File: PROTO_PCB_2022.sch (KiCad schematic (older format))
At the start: 22 parts, among them J1 HORN_EN1, J10 ECU_KILL_2, J11 ECU_KILL_3, J12 12V_EXTRA, J2 BRAKELIGHTS_EN1, J3 BRAKELIGHTS_CONN, J4 STARTER_MOTOR_EN, J5 VESC_EN_SIGNAL, J6 HORN_CONN, J7 12V_BATT1, J8 ECU_POWER_DIST, J9 ECU_KILL_1, Q1 HORN_MOSFET1, Q2 BRAKELIGHTS_MOSFET1, U1 LD1117S50TR_SOT223

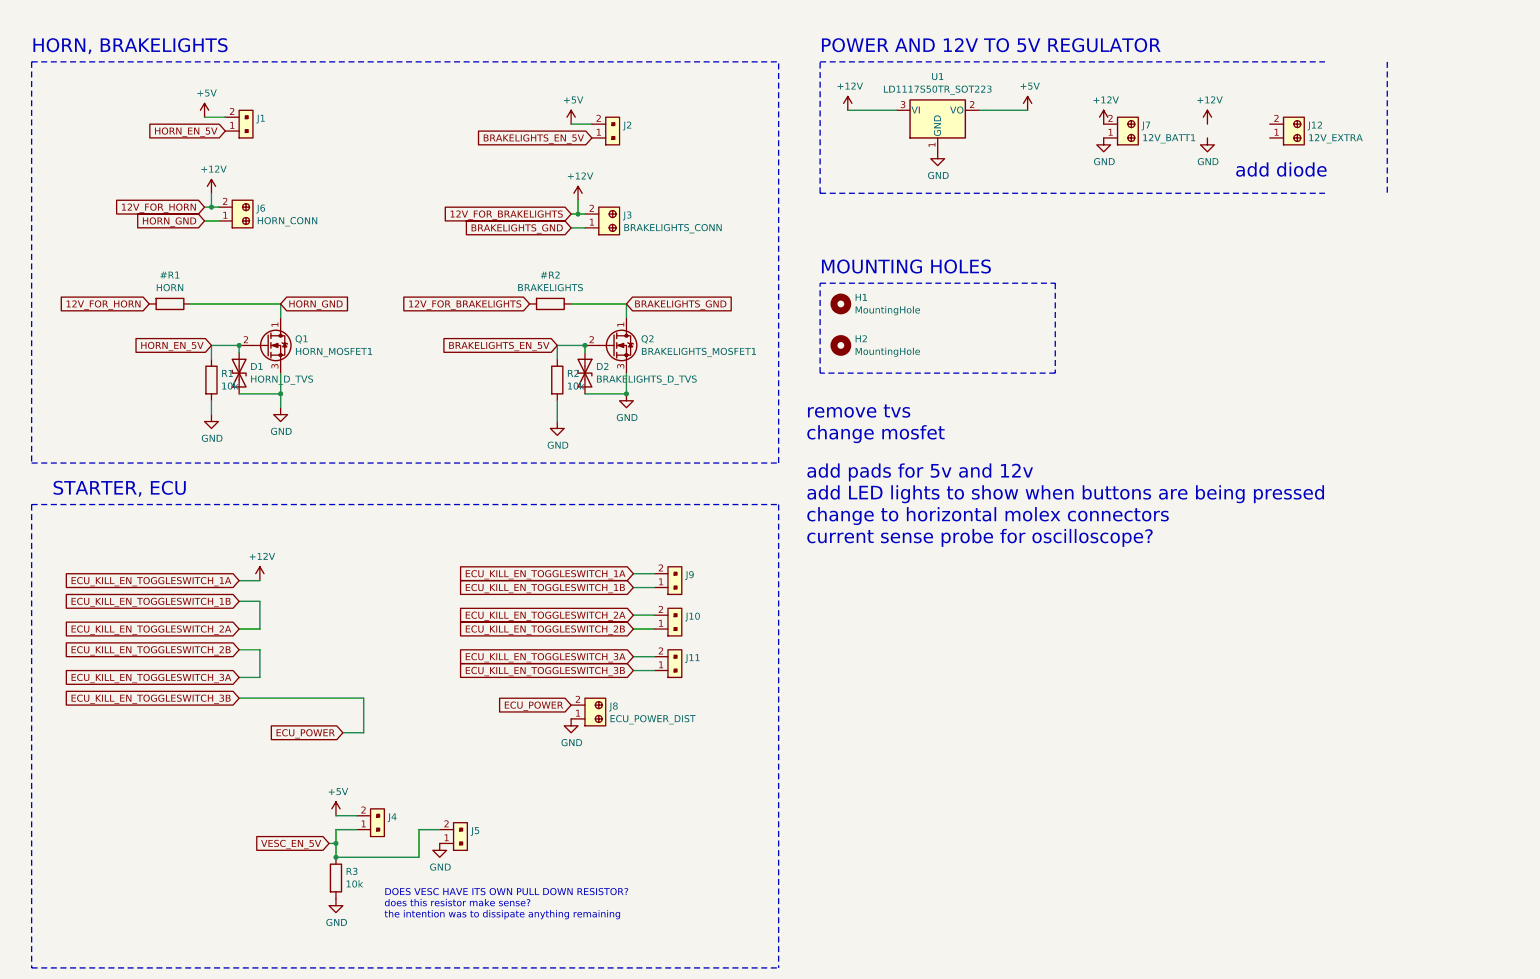
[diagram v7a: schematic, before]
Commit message: after design review edits start
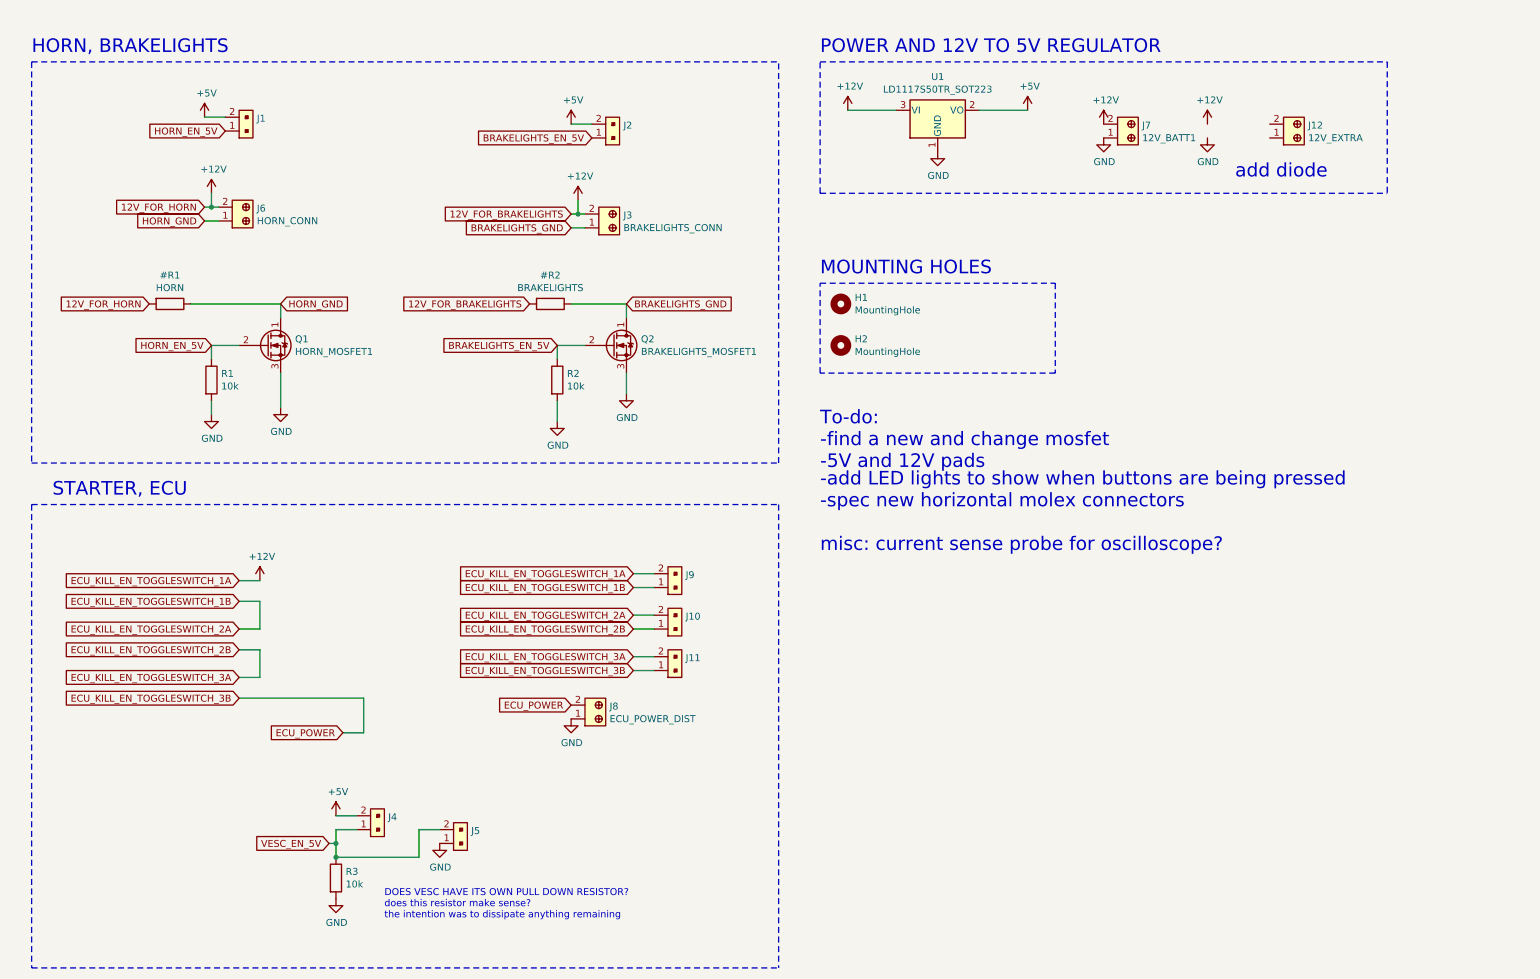
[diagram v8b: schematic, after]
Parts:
- removed D1: HORN_D_TVS, Diode_SMD:D_SMB, symbol Device:D_TVS
- removed D2: BRAKELIGHTS_D_TVS, Diode_SMD:D_SMB, symbol Device:D_TVS
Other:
- note added: "-add LED lights to show when buttons are being pressed\n-spec new horizontal molex connectors\n\nmisc: current sense probe for oscilloscope?"
- note added: "To-do:\n-find a new and change mosfet\n-5V and 12V pads\n"
- note removed: "add pads for 5v and 12v\nadd LED lights to show when buttons are being pressed\nchange to horizontal molex connectors\ncurrent sense probe for oscilloscope?"
- note removed: "remove tvs\nchange mosfet"
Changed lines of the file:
@@
 $EndComp
-$Comp
-L Device:D_TVS D2
-U 1 1 622E5E5E
-P 4800 3150
-F 0 "D2" V 4754 3230 50  0000 L CNN
-F 1 "BRAKELIGHTS_D_TVS" V 4845 3230 50  0000 L CNN
-F 2 "Diode_SMD:D_SMB" H 4800 3150 50  0001 C CNN
-F 3 "https://media.digikey.com/pdf/Data%20Sheets/AVX%20PDFs/Transient%20Suppression%20Diodes.pdf~" H 4800 3150 50  0001 C CNN
-	1    4800 3150
-	0    1    1    0
-$EndComp
-Wire Wire Line
-	4800 3000 4800 2950
-Wire Wire Line
-	4800 3300 5100 3300
-$Comp
-L Device:D_TVS D1
-U 1 1 62314A6C
-P 2300 3150
-F 0 "D1" V 2346 3070 50  0000 R CNN
-F 1 "HORN_D_TVS" V 2255 3070 50  0000 R CNN
-F 2 "Diode_SMD:D_SMB" H 2300 3150 50  0001 C CNN
-F 3 "https://media.digikey.com/pdf/Data%20Sheets/AVX%20PDFs/Transient%20Suppression%20Diodes.pdf" H 2300 3150 50  0001 C CNN
-	1    2300 3150
-	0    -1   -1   0
-$EndComp
-Wire Wire Line
-	2300 3000 2300 2950
 $Comp
 L power:GND #PWR020
@@
 Wire Wire Line
 	5100 3150 5100 3300
-Connection ~ 5100 3300
-Connection ~ 4800 2950
-$Comp
-L Device:Q_NMOS_DGS Q2
-U 1 1 618C50B5
-P 5000 2950
-F 0 "Q2" H 5205 2996 50  0000 L CNN
-F 1 "BRAKELIGHTS_MOSFET1" H 5205 2905 50  0000 L CNN
-F 2 "Package_TO_SOT_SMD:SOT-23" H 5200 3050 50  0001 C CNN
-F 3 "https://www.digikey.ca/en/products/detail/rohm-semiconductor/RK7002BMT116/4924083" H 5000 2950 50  0001 C CNN
-F 4 "RK7002BMT116" H 5000 2950 50  0001 C CNN "MPN"
-F 5 "RK7002BMT116CT-ND" H 5000 2950 50  0001 C CNN "DigiKeyPN"
-	1    5000 2950
-	1    0    0    -1
-$EndComp
 Wire Wire Line
 	5100 2650 5100 2750
@@
 Wire Notes Line
 	6500 3150 6500 2500
-Wire Notes Line
-	6500 900  10150 900
-Wire Notes Line
-	6500 1850 10150 1850
 Text GLabel 2200 1400 0    50   Input ~ 0
 HORN_EN_5V
@@
 Text GLabel 4700 5550 0    50   Input ~ 0
 ECU_POWER
-Text Notes 6400 4400 0    98   ~ 0
-add pads for 5v and 12v\nadd LED lights to show when buttons are being pressed\nchange to horizontal molex connectors\ncurrent sense probe for oscilloscope?
-Connection ~ 2300 2950
 $Comp
 L Device:Q_NMOS_DGS Q1
@@
 Text GLabel 2600 2650 2    50   Input ~ 0
 HORN_GND
-Connection ~ 2600 3300
-Wire Wire Line
-	2600 3150 2600 3300
-Wire Wire Line
-	2300 3300 2600 3300
 $Comp
 L power:GND #PWR010
@@
 $EndComp
 Wire Wire Line
-	2600 3300 2600 3400
-Wire Wire Line
 	2600 2750 2600 2650
-Text Notes 6400 3650 0    98   ~ 0
-remove tvs\nchange mosfet
+Text Notes 6500 3850 0    98   ~ 0
+To-do:\n-find a new and change mosfet\n-5V and 12V pads\n
 Text Notes 9500 1750 0    98   ~ 0
 add diode
+Wire Notes Line
+	6500 900  10600 900
+Wire Notes Line
+	6500 1850 10600 1850
+$Comp
+L Device:Q_NMOS_DGS Q2
+U 1 1 618C50B5
+P 5000 2950
+F 0 "Q2" H 5205 2996 50  0000 L CNN
+F 1 "BRAKELIGHTS_MOSFET1" H 5205 2905 50  0000 L CNN
+F 2 "Package_TO_SOT_SMD:SOT-23" H 5200 3050 50  0001 C CNN
+F 3 "https://www.digikey.ca/en/products/detail/rohm-semiconductor/RK7002BMT116/4924083" H 5000 2950 50  0001 C CNN
+F 4 "RK7002BMT116" H 5000 2950 50  0001 C CNN "MPN"
+F 5 "RK7002BMT116CT-ND" H 5000 2950 50  0001 C CNN "DigiKeyPN"
+	1    5000 2950
+	1    0    0    -1
+$EndComp
+Wire Wire Line
+	2600 3150 2600 3400
+Text Notes 6500 4450 0    98   ~ 0
+-add LED lights to show when buttons are being pressed\n-spec new horizontal molex connectors\n\nmisc: current sense probe for oscilloscope?
 $EndSCHEMATC
